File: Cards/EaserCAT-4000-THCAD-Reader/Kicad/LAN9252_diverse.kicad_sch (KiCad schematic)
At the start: 58 parts, among them U2 AT24CS32-SSHM

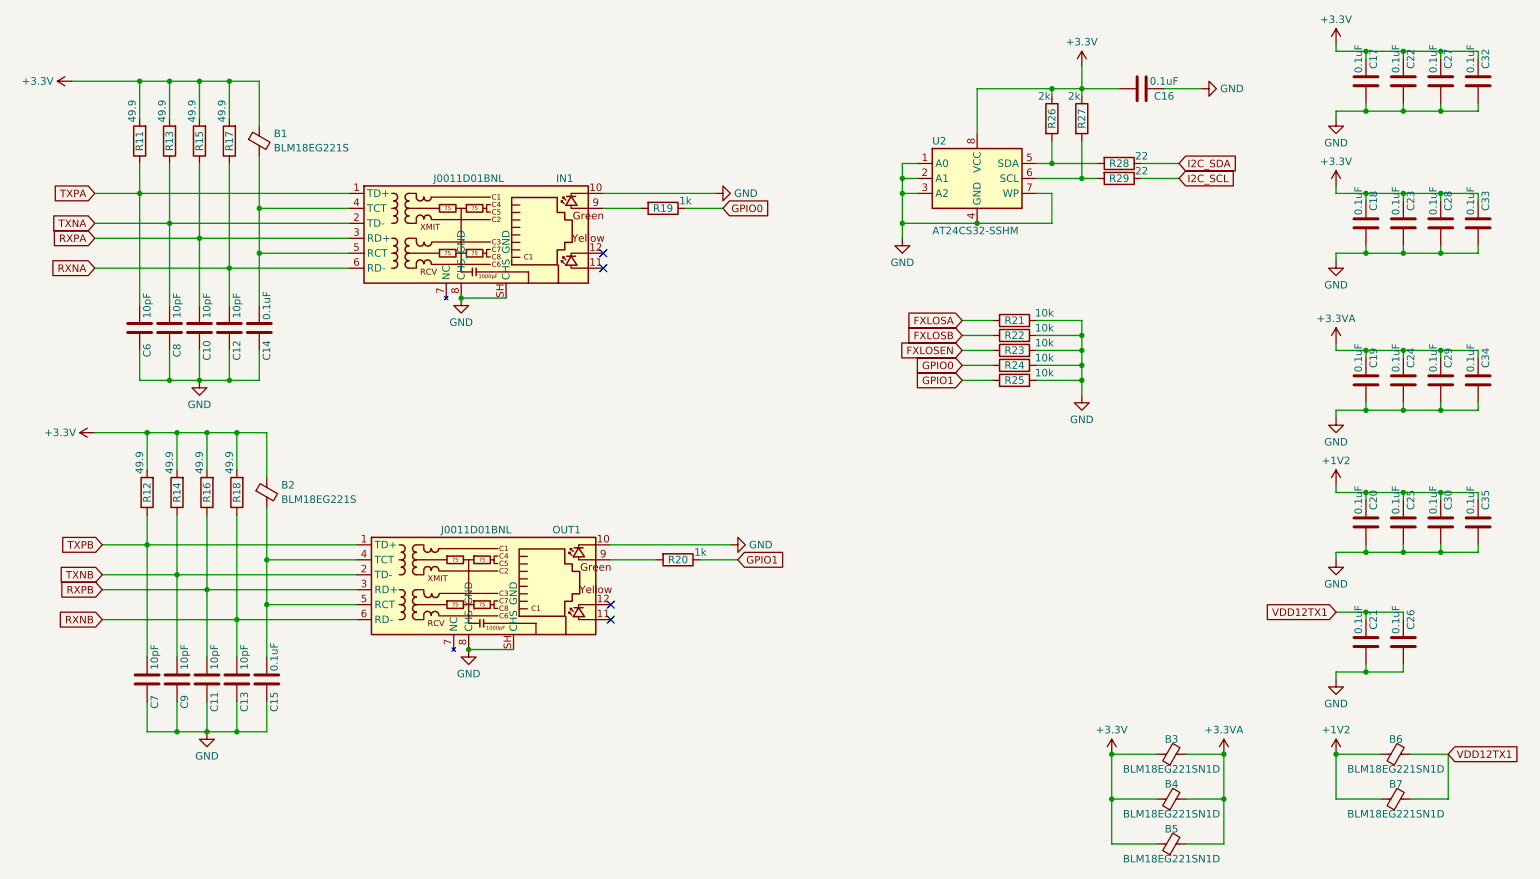
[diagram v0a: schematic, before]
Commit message: Moving all to Kicad8. Housekeeping symbols,libraries,3d-models
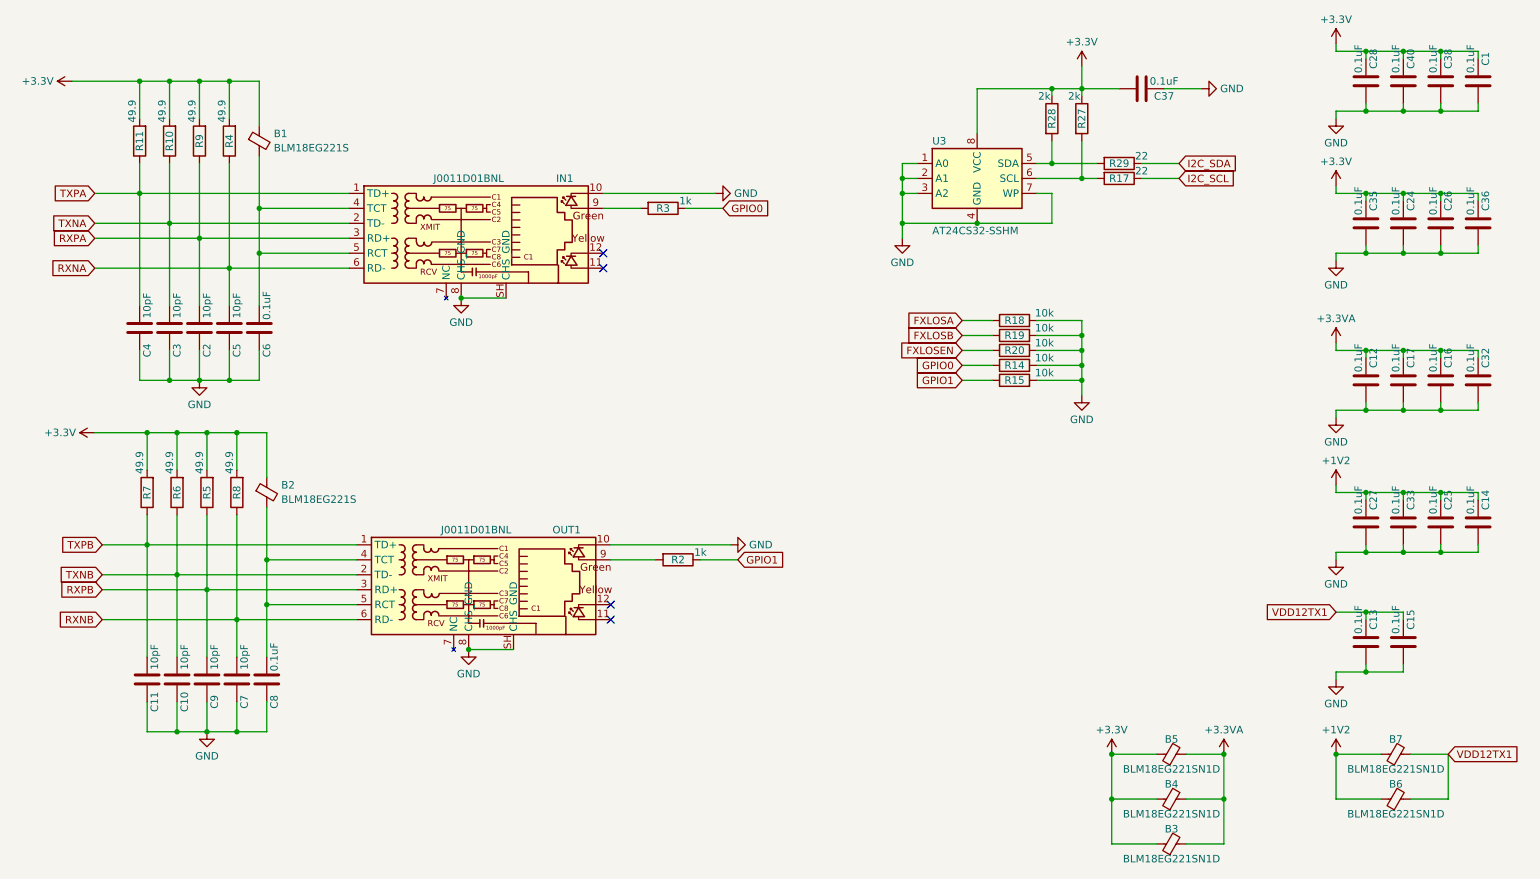
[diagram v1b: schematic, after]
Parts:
- renumbered B5 to B3, B3 to B5, B7 to B6, B6 to B7, C32 to C1, C9 to C10, C7 to C11, C19 to C12, C21 to C13, C35 to C14, C26 to C15, C29 to C16, C24 to C17, C10 to C2, C23 to C24, C30 to C25, C28 to C26, C20 to C27, C17 to C28, C8 to C3, C34 to C32, C25 to C33, C18 to C35, C33 to C36, C16 to C37, C27 to C38, C6 to C4, C22 to C40, C12 to C5, C14 to C6, C13 to C7, C15 to C8, C11 to C9, R13 to R10, R24 to R14, R25 to R15, R29 to R17, R21 to R18, R22 to R19, R20 to R2, R23 to R20, R26 to R28, R28 to R29, R19 to R3, R17 to R4, R16 to R5, R14 to R6, R12 to R7, R18 to R8, R15 to R9, U2 to U3
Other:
- title: (none) -> THCAD reader
